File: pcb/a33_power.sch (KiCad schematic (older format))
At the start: 63 parts, among them U3 TPS62095RGTR, U4 TPS62095RGTR, U5 TPS62095RGTR, U6 TPS62095RGTR, U7 AP131-25

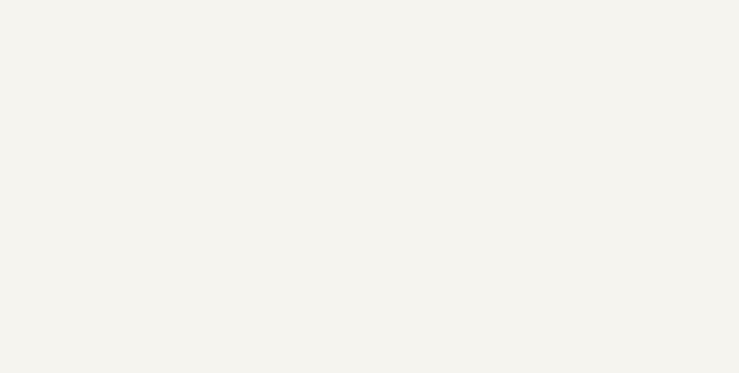
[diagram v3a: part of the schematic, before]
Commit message: Added in the mains to 5V module, this will most likely be removed in the future.
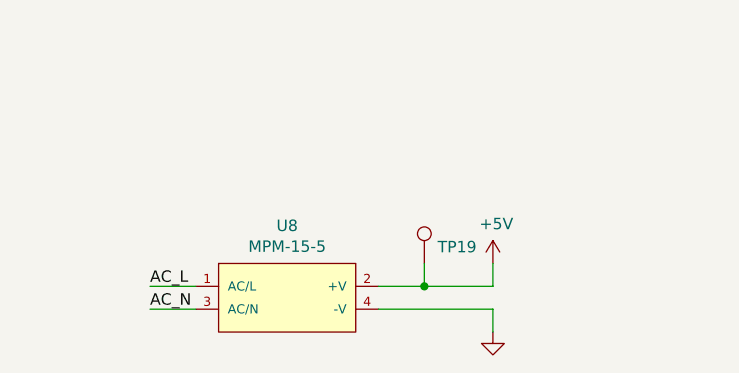
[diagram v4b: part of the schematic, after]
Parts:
- added TP19: TestPoint, TestPoint:TestPoint_Pad_1.0x1.0mm, symbol Connector:TestPoint
- added U8: MPM-15-5, MEAN_WELL-MPM-15-5-*, symbol MPM-15-5:MPM-15-5
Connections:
- net +5V: now also TP19.1, U8.2 (+V)
- net GND: now also U8.4 (-V)
- new net AC_L: U8.1 (AC/L)
- new net AC_N: U8.3 (AC/N)
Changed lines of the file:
@@
 Wire Wire Line
 	4800 5650 4550 5650
+$Comp
+L MPM-15-5:MPM-15-5 U8
+U 1 1 60F3A4A1
+P 1300 6650
+F 0 "U8" H 1800 6915 50  0000 C CNN
+F 1 "MPM-15-5" H 1800 6824 50  0000 C CNN
+F 2 "MEAN_WELL-MPM-15-5-*" H 1300 7050 50  0001 L CNN
+F 3 "https://www.meanwell.com/webapp/product/search.aspx?prod=MPM-15#1" H 1300 7150 50  0001 L CNN
+F 4 "No" H 1300 7250 50  0001 L CNN "automotive"
+F 5 "IC" H 1300 7350 50  0001 L CNN "category"
+F 6 "Integrated Circuits (ICs)" H 1300 7450 50  0001 L CNN "device class L1"
+F 7 "Power Management ICs" H 1300 7550 50  0001 L CNN "device class L2"
+F 8 "unset" H 1300 7650 50  0001 L CNN "device class L3"
+F 9 "AC/DC CONVERTER 5V 15W" H 1300 7750 50  0001 L CNN "digikey description"
+F 10 "1866-5334-ND" H 1300 7850 50  0001 L CNN "digikey part number"
+F 11 "24mm" H 1300 7950 50  0001 L CNN "height"
+F 12 "Yes" H 1300 8050 50  0001 L CNN "lead free"
+F 13 "07bef24d1664adcc" H 1300 8150 50  0001 L CNN "library id"
+F 14 "MEAN WELL" H 1300 8250 50  0001 L CNN "manufacturer"
+F 15 "15W" H 1300 8350 50  0001 L CNN "max power dissipation"
+F 16 "264V" H 1300 8450 50  0001 L CNN "max supply voltage"
+F 17 "80V" H 1300 8550 50  0001 L CNN "min supply voltage"
+F 18 "709-MPM-15-5" H 1300 8650 50  0001 L CNN "mouser part number"
+F 19 "0.3-0.6A" H 1300 8750 50  0001 L CNN "nominal supply current"
+F 20 "1" H 1300 8850 50  0001 L CNN "number of outputs"
+F 21 "3A" H 1300 8950 50  0001 L CNN "output current"
+F 22 "5V" H 1300 9050 50  0001 L CNN "output voltage"
+F 23 "DIP4" H 1300 9150 50  0001 L CNN "package"
+F 24 "Yes" H 1300 9250 50  0001 L CNN "rohs"
+F 25 "+85°C" H 1300 9350 50  0001 L CNN "temperature range high"
+F 26 "-40°C" H 1300 9450 50  0001 L CNN "temperature range low"
+F 27 "MPM-15-5" H 1300 6650 50  0001 C CNN "Part Number"
+	1    1300 6650
+	1    0    0    -1
+$EndComp
+Wire Wire Line
+	1400 6650 1200 6650
+Wire Wire Line
+	1400 6750 1200 6750
+Text Label 1200 6650 0    50   ~ 0
+AC_L
+Text Label 1200 6750 0    50   ~ 0
+AC_N
+$Comp
+L power:+5V #PWR070
+U 1 1 60F7B9D6
+P 2700 6550
+F 0 "#PWR070" H 2700 6400 50  0001 C CNN
+F 1 "+5V" H 2715 6723 50  0000 C CNN
+F 2 "" H 2700 6550 50  0001 C CNN
+F 3 "" H 2700 6550 50  0001 C CNN
+	1    2700 6550
+	1    0    0    -1
+$EndComp
+$Comp
+L power:GND #PWR?
+U 1 1 60F96CCE
+P 2700 6850
+AR Path="/60536DA4/60F96CCE" Ref="#PWR?"  Part="1"
+AR Path="/60F96CCE" Ref="#PWR?"  Part="1"
+AR Path="/60A30BFF/60F96CCE" Ref="#PWR071"  Part="1"
+F 0 "#PWR071" H 2700 6600 50  0001 C CNN
+F 1 "GND" V 2705 6722 50  0001 R CNN
+F 2 "" H 2700 6850 50  0001 C CNN
+F 3 "" H 2700 6850 50  0001 C CNN
+	1    2700 6850
+	1    0    0    -1
+$EndComp
+Wire Wire Line
+	2200 6650 2400 6650
+Wire Wire Line
+	2700 6650 2700 6550
+Wire Wire Line
+	2200 6750 2700 6750
+Wire Wire Line
+	2700 6750 2700 6850
+$Comp
+L Connector:TestPoint TP19
+U 1 1 60FBE2BB
+P 2400 6550
+F 0 "TP19" H 2458 6622 50  0000 L CNN
+F 1 "TestPoint" H 2458 6577 50  0001 L CNN
+F 2 "TestPoint:TestPoint_Pad_1.0x1.0mm" H 2600 6550 50  0001 C CNN
+F 3 "~" H 2600 6550 50  0001 C CNN
+	1    2400 6550
+	1    0    0    -1
+$EndComp
+Wire Wire Line
+	2400 6650 2400 6550
+Connection ~ 2400 6650
+Wire Wire Line
+	2400 6650 2700 6650
 $EndSCHEMATC

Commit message: Figured out all the crystals
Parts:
- U8: footprint MEAN_WELL-MPM-15-5-* -> MPM-15-5:MEAN_WELL-MPM-15-5-MFG
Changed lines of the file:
@@
 F 0 "U8" H 1800 6915 50  0000 C CNN
 F 1 "MPM-15-5" H 1800 6824 50  0000 C CNN
-F 2 "MEAN_WELL-MPM-15-5-*" H 1300 7050 50  0001 L CNN
+F 2 "MPM-15-5:MEAN_WELL-MPM-15-5-MFG" H 1300 7050 50  0001 L CNN
 F 3 "https://www.meanwell.com/webapp/product/search.aspx?prod=MPM-15#1" H 1300 7150 50  0001 L CNN
 F 4 "No" H 1300 7250 50  0001 L CNN "automotive"

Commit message: Backing up
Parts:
- C10, C11, C12, C13, C14, C15, C16, C17, C18, C19, C20, C21, C22, C23, C24, C25, C26, C27, C28, C6, C7, C8, C9: footprint Capacitor_SMD:C_01005_0402Metric -> Capacitor_SMD:C_0402_1005Metric
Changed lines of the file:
@@
 F 0 "C9" H 4250 1300 50  0000 L CNN
 F 1 "22uF" H 4250 1100 50  0000 L CNN
-F 2 "Capacitor_SMD:C_01005_0402Metric" H 4200 1200 50  0001 C CNN
+F 2 "Capacitor_SMD:C_0402_1005Metric" H 4200 1200 50  0001 C CNN
 F 3 "~" H 4200 1200 50  0001 C CNN
 	1    4200 1200
@@
 F 0 "C10" H 4550 1300 50  0000 L CNN
 F 1 "22uF" H 4550 1100 50  0000 L CNN
-F 2 "Capacitor_SMD:C_01005_0402Metric" H 4500 1200 50  0001 C CNN
+F 2 "Capacitor_SMD:C_0402_1005Metric" H 4500 1200 50  0001 C CNN
 F 3 "~" H 4500 1200 50  0001 C CNN
 	1    4500 1200
@@
 F 0 "C7" H 3200 1950 50  0000 L CNN
 F 1 "10nF" H 3200 1750 50  0000 L CNN
-F 2 "Capacitor_SMD:C_01005_0402Metric" H 3150 1850 50  0001 C CNN
+F 2 "Capacitor_SMD:C_0402_1005Metric" H 3150 1850 50  0001 C CNN
 F 3 "~" H 3150 1850 50  0001 C CNN
 	1    3150 1850
@@
 F 0 "C8" H 3200 2550 50  0000 L CNN
 F 1 "450pF" H 3200 2350 50  0000 L CNN
-F 2 "Capacitor_SMD:C_01005_0402Metric" H 3150 2450 50  0001 C CNN
+F 2 "Capacitor_SMD:C_0402_1005Metric" H 3150 2450 50  0001 C CNN
 F 3 "~" H 3150 2450 50  0001 C CNN
 	1    3150 2450
@@
 F 0 "C6" H 950 1300 50  0000 L CNN
 F 1 "22uF" H 950 1100 50  0000 L CNN
-F 2 "Capacitor_SMD:C_01005_0402Metric" H 900 1200 50  0001 C CNN
+F 2 "Capacitor_SMD:C_0402_1005Metric" H 900 1200 50  0001 C CNN
 F 3 "~" H 900 1200 50  0001 C CNN
 	1    900  1200
@@
 F 0 "C14" H 4250 3650 50  0000 L CNN
 F 1 "22uF" H 4250 3450 50  0000 L CNN
-F 2 "Capacitor_SMD:C_01005_0402Metric" H 4200 3550 50  0001 C CNN
+F 2 "Capacitor_SMD:C_0402_1005Metric" H 4200 3550 50  0001 C CNN
 F 3 "~" H 4200 3550 50  0001 C CNN
 	1    4200 3550
@@
 F 0 "C15" H 4550 3650 50  0000 L CNN
 F 1 "22uF" H 4550 3450 50  0000 L CNN
-F 2 "Capacitor_SMD:C_01005_0402Metric" H 4500 3550 50  0001 C CNN
+F 2 "Capacitor_SMD:C_0402_1005Metric" H 4500 3550 50  0001 C CNN
 F 3 "~" H 4500 3550 50  0001 C CNN
 	1    4500 3550
@@
 F 0 "C12" H 3200 4300 50  0000 L CNN
 F 1 "10nF" H 3200 4100 50  0000 L CNN
-F 2 "Capacitor_SMD:C_01005_0402Metric" H 3150 4200 50  0001 C CNN
+F 2 "Capacitor_SMD:C_0402_1005Metric" H 3150 4200 50  0001 C CNN
 F 3 "~" H 3150 4200 50  0001 C CNN
 	1    3150 4200
@@
 F 0 "C13" H 3200 4900 50  0000 L CNN
 F 1 "450pF" H 3200 4700 50  0000 L CNN
-F 2 "Capacitor_SMD:C_01005_0402Metric" H 3150 4800 50  0001 C CNN
+F 2 "Capacitor_SMD:C_0402_1005Metric" H 3150 4800 50  0001 C CNN
 F 3 "~" H 3150 4800 50  0001 C CNN
 	1    3150 4800
@@
 F 0 "C11" H 950 3650 50  0000 L CNN
 F 1 "22uF" H 950 3450 50  0000 L CNN
-F 2 "Capacitor_SMD:C_01005_0402Metric" H 900 3550 50  0001 C CNN
+F 2 "Capacitor_SMD:C_0402_1005Metric" H 900 3550 50  0001 C CNN
 F 3 "~" H 900 3550 50  0001 C CNN
 	1    900  3550
@@
 F 0 "C22" H 9500 1300 50  0000 L CNN
 F 1 "22uF" H 9500 1100 50  0000 L CNN
-F 2 "Capacitor_SMD:C_01005_0402Metric" H 9450 1200 50  0001 C CNN
+F 2 "Capacitor_SMD:C_0402_1005Metric" H 9450 1200 50  0001 C CNN
 F 3 "~" H 9450 1200 50  0001 C CNN
 	1    9450 1200
@@
 F 0 "C24" H 9800 1300 50  0000 L CNN
 F 1 "22uF" H 9800 1100 50  0000 L CNN
-F 2 "Capacitor_SMD:C_01005_0402Metric" H 9750 1200 50  0001 C CNN
+F 2 "Capacitor_SMD:C_0402_1005Metric" H 9750 1200 50  0001 C CNN
 F 3 "~" H 9750 1200 50  0001 C CNN
 	1    9750 1200
@@
 F 0 "C18" H 8450 1950 50  0000 L CNN
 F 1 "10nF" H 8450 1750 50  0000 L CNN
-F 2 "Capacitor_SMD:C_01005_0402Metric" H 8400 1850 50  0001 C CNN
+F 2 "Capacitor_SMD:C_0402_1005Metric" H 8400 1850 50  0001 C CNN
 F 3 "~" H 8400 1850 50  0001 C CNN
 	1    8400 1850
@@
 F 0 "C19" H 8450 2550 50  0000 L CNN
 F 1 "5nF" H 8450 2350 50  0000 L CNN
-F 2 "Capacitor_SMD:C_01005_0402Metric" H 8400 2450 50  0001 C CNN
+F 2 "Capacitor_SMD:C_0402_1005Metric" H 8400 2450 50  0001 C CNN
 F 3 "~" H 8400 2450 50  0001 C CNN
 	1    8400 2450
@@
 F 0 "C16" H 6200 1300 50  0000 L CNN
 F 1 "22uF" H 6200 1100 50  0000 L CNN
-F 2 "Capacitor_SMD:C_01005_0402Metric" H 6150 1200 50  0001 C CNN
+F 2 "Capacitor_SMD:C_0402_1005Metric" H 6150 1200 50  0001 C CNN
 F 3 "~" H 6150 1200 50  0001 C CNN
 	1    6150 1200
@@
 F 0 "C23" H 9500 3500 50  0000 L CNN
 F 1 "22uF" H 9500 3300 50  0000 L CNN
-F 2 "Capacitor_SMD:C_01005_0402Metric" H 9450 3400 50  0001 C CNN
+F 2 "Capacitor_SMD:C_0402_1005Metric" H 9450 3400 50  0001 C CNN
 F 3 "~" H 9450 3400 50  0001 C CNN
 	1    9450 3400
@@
 F 0 "C25" H 9800 3500 50  0000 L CNN
 F 1 "22uF" H 9800 3300 50  0000 L CNN
-F 2 "Capacitor_SMD:C_01005_0402Metric" H 9750 3400 50  0001 C CNN
+F 2 "Capacitor_SMD:C_0402_1005Metric" H 9750 3400 50  0001 C CNN
 F 3 "~" H 9750 3400 50  0001 C CNN
 	1    9750 3400
@@
 F 0 "C20" H 8450 4150 50  0000 L CNN
 F 1 "10nF" H 8450 3950 50  0000 L CNN
-F 2 "Capacitor_SMD:C_01005_0402Metric" H 8400 4050 50  0001 C CNN
+F 2 "Capacitor_SMD:C_0402_1005Metric" H 8400 4050 50  0001 C CNN
 F 3 "~" H 8400 4050 50  0001 C CNN
 	1    8400 4050
@@
 F 0 "C21" H 8450 4750 50  0000 L CNN
 F 1 "5nF" H 8450 4550 50  0000 L CNN
-F 2 "Capacitor_SMD:C_01005_0402Metric" H 8400 4650 50  0001 C CNN
+F 2 "Capacitor_SMD:C_0402_1005Metric" H 8400 4650 50  0001 C CNN
 F 3 "~" H 8400 4650 50  0001 C CNN
 	1    8400 4650
@@
 F 0 "C17" H 6200 3500 50  0000 L CNN
 F 1 "22uF" H 6200 3300 50  0000 L CNN
-F 2 "Capacitor_SMD:C_01005_0402Metric" H 6150 3400 50  0001 C CNN
+F 2 "Capacitor_SMD:C_0402_1005Metric" H 6150 3400 50  0001 C CNN
 F 3 "~" H 6150 3400 50  0001 C CNN
 	1    6150 3400
@@
 F 0 "C28" H 6000 6050 50  0000 L CNN
 F 1 "10uF" H 6000 5850 50  0000 L CNN
-F 2 "Capacitor_SMD:C_01005_0402Metric" H 5950 5950 50  0001 C CNN
+F 2 "Capacitor_SMD:C_0402_1005Metric" H 5950 5950 50  0001 C CNN
 F 3 "~" H 5950 5950 50  0001 C CNN
 	1    5950 5950
@@
 F 0 "C27" H 5650 6050 50  0000 L CNN
 F 1 "0.1uF" H 5650 5850 50  0000 L CNN
-F 2 "Capacitor_SMD:C_01005_0402Metric" H 5600 5950 50  0001 C CNN
+F 2 "Capacitor_SMD:C_0402_1005Metric" H 5600 5950 50  0001 C CNN
 F 3 "~" H 5600 5950 50  0001 C CNN
 	1    5600 5950
@@
 F 0 "C26" H 4600 5950 50  0000 L CNN
 F 1 "10uF" H 4600 5750 50  0000 L CNN
-F 2 "Capacitor_SMD:C_01005_0402Metric" H 4550 5850 50  0001 C CNN
+F 2 "Capacitor_SMD:C_0402_1005Metric" H 4550 5850 50  0001 C CNN
 F 3 "~" H 4550 5850 50  0001 C CNN
 	1    4550 5850

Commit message: Working on the layout
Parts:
- removed TP19, TP4, TP7, TP8: TestPoint, TestPoint:TestPoint_Pad_1.0x1.0mm, symbol Connector:TestPoint
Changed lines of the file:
@@
 Connection ~ 900  3350
-Wire Wire Line
-	900  3350 1150 3350
 Wire Wire Line
 	900  3650 900  3750
@@
 Wire Wire Line
 	4700 3350 4700 3200
-$Comp
-L Connector:TestPoint TP4
-U 1 1 60A665AC
-P 1150 3200
-F 0 "TP4" H 1208 3272 50  0000 L CNN
-F 1 "TestPoint" H 1208 3227 50  0001 L CNN
-F 2 "TestPoint:TestPoint_Pad_1.0x1.0mm" H 1350 3200 50  0001 C CNN
-F 3 "~" H 1350 3200 50  0001 C CNN
-	1    1150 3200
-	1    0    0    -1
-$EndComp
-Wire Wire Line
-	1150 3350 1150 3200
-Connection ~ 1150 3350
-Wire Wire Line
-	1150 3350 1350 3350
 $Comp
 L power:+5V #PWR029
@@
 Connection ~ 6150 1000
 Wire Wire Line
-	6150 1000 6400 1000
-Wire Wire Line
 	6150 1300 6150 1400
 $Comp
@@
 Wire Wire Line
 	9950 1000 9950 850
-$Comp
-L Connector:TestPoint TP7
-U 1 1 60A89518
-P 6400 850
-F 0 "TP7" H 6458 922 50  0000 L CNN
-F 1 "TestPoint" H 6458 877 50  0001 L CNN
-F 2 "TestPoint:TestPoint_Pad_1.0x1.0mm" H 6600 850 50  0001 C CNN
-F 3 "~" H 6600 850 50  0001 C CNN
-	1    6400 850
-	1    0    0    -1
-$EndComp
-Wire Wire Line
-	6400 1000 6400 850
-Connection ~ 6400 1000
-Wire Wire Line
-	6400 1000 6600 1000
 $Comp
 L power:+5V #PWR030
@@
 Connection ~ 6150 3200
 Wire Wire Line
-	6150 3200 6400 3200
-Wire Wire Line
 	6150 3500 6150 3600
 $Comp
@@
 Wire Wire Line
 	9950 3200 9950 3050
-$Comp
-L Connector:TestPoint TP8
-U 1 1 60C5312A
-P 6400 3050
-F 0 "TP8" H 6458 3122 50  0000 L CNN
-F 1 "TestPoint" H 6458 3077 50  0001 L CNN
-F 2 "TestPoint:TestPoint_Pad_1.0x1.0mm" H 6600 3050 50  0001 C CNN
-F 3 "~" H 6600 3050 50  0001 C CNN
-	1    6400 3050
-	1    0    0    -1
-$EndComp
-Wire Wire Line
-	6400 3200 6400 3050
-Connection ~ 6400 3200
-Wire Wire Line
-	6400 3200 6600 3200
 $Comp
 L power:+3V0 #PWR028
@@
 $EndComp
 Wire Wire Line
-	2200 6650 2400 6650
-Wire Wire Line
 	2700 6650 2700 6550
 Wire Wire Line
@@
 Wire Wire Line
 	2700 6750 2700 6850
-$Comp
-L Connector:TestPoint TP19
-U 1 1 60FBE2BB
-P 2400 6550
-F 0 "TP19" H 2458 6622 50  0000 L CNN
-F 1 "TestPoint" H 2458 6577 50  0001 L CNN
-F 2 "TestPoint:TestPoint_Pad_1.0x1.0mm" H 2600 6550 50  0001 C CNN
-F 3 "~" H 2600 6550 50  0001 C CNN
-	1    2400 6550
-	1    0    0    -1
-$EndComp
-Wire Wire Line
-	2400 6650 2400 6550
-Connection ~ 2400 6650
-Wire Wire Line
-	2400 6650 2700 6650
+Wire Wire Line
+	900  3350 1350 3350
+Wire Wire Line
+	6150 3200 6600 3200
+Wire Wire Line
+	6150 1000 6600 1000
+Wire Wire Line
+	2200 6650 2700 6650
 $EndSCHEMATC

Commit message: Working on the power supplies
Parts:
- removed TP10, TP2, TP5, TP9: TestPoint, TestPoint:TestPoint_Pad_1.0x1.0mm, symbol Connector:TestPoint
- C10, C11, C14, C15, C16, C17, C22, C23, C24, C25, C26, C28, C6, C9: footprint Capacitor_SMD:C_0402_1005Metric -> Capacitor_SMD:C_0805_2012Metric
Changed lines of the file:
@@
 	1350 2100 1350 1300
 Connection ~ 1350 1300
-$Comp
-L Connector:TestPoint TP2
-U 1 1 6077F3FF
-P 1450 1800
-F 0 "TP2" H 1508 1872 50  0000 L CNN
-F 1 "TestPoint" H 1508 1827 50  0001 L CNN
-F 2 "TestPoint:TestPoint_Pad_1.0x1.0mm" H 1650 1800 50  0001 C CNN
-F 3 "~" H 1650 1800 50  0001 C CNN
-	1    1450 1800
-	1    0    0    -1
-$EndComp
 Connection ~ 1350 1000
 Wire Wire Line
@@
 Wire Wire Line
 	1350 2100 1550 2100
-Wire Wire Line
-	1550 1900 1450 1900
-Wire Wire Line
-	1450 1900 1450 1800
 Wire Wire Line
 	2950 1100 3050 1100
@@
 F 0 "C9" H 4250 1300 50  0000 L CNN
 F 1 "22uF" H 4250 1100 50  0000 L CNN
-F 2 "Capacitor_SMD:C_0402_1005Metric" H 4200 1200 50  0001 C CNN
+F 2 "Capacitor_SMD:C_0805_2012Metric" H 4200 1200 50  0001 C CNN
 F 3 "~" H 4200 1200 50  0001 C CNN
 	1    4200 1200
@@
 F 0 "C10" H 4550 1300 50  0000 L CNN
 F 1 "22uF" H 4550 1100 50  0000 L CNN
-F 2 "Capacitor_SMD:C_0402_1005Metric" H 4500 1200 50  0001 C CNN
+F 2 "Capacitor_SMD:C_0805_2012Metric" H 4500 1200 50  0001 C CNN
 F 3 "~" H 4500 1200 50  0001 C CNN
 	1    4500 1200
@@
 F 0 "C6" H 950 1300 50  0000 L CNN
 F 1 "22uF" H 950 1100 50  0000 L CNN
-F 2 "Capacitor_SMD:C_0402_1005Metric" H 900 1200 50  0001 C CNN
+F 2 "Capacitor_SMD:C_0805_2012Metric" H 900 1200 50  0001 C CNN
 F 3 "~" H 900 1200 50  0001 C CNN
 	1    900  1200
@@
 	1350 4450 1350 3650
 Connection ~ 1350 3650
-$Comp
-L Connector:TestPoint TP5
-U 1 1 60A66511
-P 1450 4150
-F 0 "TP5" H 1508 4222 50  0000 L CNN
-F 1 "TestPoint" H 1508 4177 50  0001 L CNN
-F 2 "TestPoint:TestPoint_Pad_1.0x1.0mm" H 1650 4150 50  0001 C CNN
-F 3 "~" H 1650 4150 50  0001 C CNN
-	1    1450 4150
-	1    0    0    -1
-$EndComp
 Connection ~ 1350 3350
 Wire Wire Line
@@
 Wire Wire Line
 	1350 4450 1550 4450
-Wire Wire Line
-	1550 4250 1450 4250
-Wire Wire Line
-	1450 4250 1450 4150
 Wire Wire Line
 	2950 3450 3050 3450
@@
 F 0 "C14" H 4250 3650 50  0000 L CNN
 F 1 "22uF" H 4250 3450 50  0000 L CNN
-F 2 "Capacitor_SMD:C_0402_1005Metric" H 4200 3550 50  0001 C CNN
+F 2 "Capacitor_SMD:C_0805_2012Metric" H 4200 3550 50  0001 C CNN
 F 3 "~" H 4200 3550 50  0001 C CNN
 	1    4200 3550
@@
 F 0 "C15" H 4550 3650 50  0000 L CNN
 F 1 "22uF" H 4550 3450 50  0000 L CNN
-F 2 "Capacitor_SMD:C_0402_1005Metric" H 4500 3550 50  0001 C CNN
+F 2 "Capacitor_SMD:C_0805_2012Metric" H 4500 3550 50  0001 C CNN
 F 3 "~" H 4500 3550 50  0001 C CNN
 	1    4500 3550
@@
 F 0 "C11" H 950 3650 50  0000 L CNN
 F 1 "22uF" H 950 3450 50  0000 L CNN
-F 2 "Capacitor_SMD:C_0402_1005Metric" H 900 3550 50  0001 C CNN
+F 2 "Capacitor_SMD:C_0805_2012Metric" H 900 3550 50  0001 C CNN
 F 3 "~" H 900 3550 50  0001 C CNN
 	1    900  3550
@@
 	6600 2100 6600 1300
 Connection ~ 6600 1300
-$Comp
-L Connector:TestPoint TP9
-U 1 1 60A8947D
-P 6700 1800
-F 0 "TP9" H 6758 1872 50  0000 L CNN
-F 1 "TestPoint" H 6758 1827 50  0001 L CNN
-F 2 "TestPoint:TestPoint_Pad_1.0x1.0mm" H 6900 1800 50  0001 C CNN
-F 3 "~" H 6900 1800 50  0001 C CNN
-	1    6700 1800
-	1    0    0    -1
-$EndComp
 Connection ~ 6600 1000
 Wire Wire Line
@@
 Wire Wire Line
 	6600 2100 6800 2100
-Wire Wire Line
-	6800 1900 6700 1900
-Wire Wire Line
-	6700 1900 6700 1800
 Wire Wire Line
 	8200 1100 8300 1100
@@
 F 0 "C22" H 9500 1300 50  0000 L CNN
 F 1 "22uF" H 9500 1100 50  0000 L CNN
-F 2 "Capacitor_SMD:C_0402_1005Metric" H 9450 1200 50  0001 C CNN
+F 2 "Capacitor_SMD:C_0805_2012Metric" H 9450 1200 50  0001 C CNN
 F 3 "~" H 9450 1200 50  0001 C CNN
 	1    9450 1200
@@
 F 0 "C24" H 9800 1300 50  0000 L CNN
 F 1 "22uF" H 9800 1100 50  0000 L CNN
-F 2 "Capacitor_SMD:C_0402_1005Metric" H 9750 1200 50  0001 C CNN
+F 2 "Capacitor_SMD:C_0805_2012Metric" H 9750 1200 50  0001 C CNN
 F 3 "~" H 9750 1200 50  0001 C CNN
 	1    9750 1200
@@
 Wire Wire Line
 	8400 2100 8400 2350
-$Comp
-L TI:TPS62095 U5
-U 1 1 60A894ED
-P 7500 1550
-F 0 "U5" H 7500 2387 60  0000 C CNN
-F 1 "TPS62095RGTR" H 7500 2281 60  0000 C CNN
-F 2 "TI:TI_RTE_S-PWQFN-N16" H 7500 1750 60  0001 C CNN
-F 3 "" H 7500 1750 60  0001 C CNN
-	1    7500 1550
-	1    0    0    -1
-$EndComp
 Wire Notes Line
 	8700 2250 7900 2250
@@
 F 0 "C16" H 6200 1300 50  0000 L CNN
 F 1 "22uF" H 6200 1100 50  0000 L CNN
-F 2 "Capacitor_SMD:C_0402_1005Metric" H 6150 1200 50  0001 C CNN
+F 2 "Capacitor_SMD:C_0805_2012Metric" H 6150 1200 50  0001 C CNN
 F 3 "~" H 6150 1200 50  0001 C CNN
 	1    6150 1200
@@
 	6600 4300 6600 3500
 Connection ~ 6600 3500
-$Comp
-L Connector:TestPoint TP10
-U 1 1 60C5308F
-P 6700 4000
-F 0 "TP10" H 6758 4072 50  0000 L CNN
-F 1 "TestPoint" H 6758 4027 50  0001 L CNN
-F 2 "TestPoint:TestPoint_Pad_1.0x1.0mm" H 6900 4000 50  0001 C CNN
-F 3 "~" H 6900 4000 50  0001 C CNN
-	1    6700 4000
-	1    0    0    -1
-$EndComp
 Connection ~ 6600 3200
 Wire Wire Line
@@
 Wire Wire Line
 	6600 4300 6800 4300
-Wire Wire Line
-	6800 4100 6700 4100
-Wire Wire Line
-	6700 4100 6700 4000
 Wire Wire Line
 	8200 3300 8300 3300
@@
 F 0 "C23" H 9500 3500 50  0000 L CNN
 F 1 "22uF" H 9500 3300 50  0000 L CNN
-F 2 "Capacitor_SMD:C_0402_1005Metric" H 9450 3400 50  0001 C CNN
+F 2 "Capacitor_SMD:C_0805_2012Metric" H 9450 3400 50  0001 C CNN
 F 3 "~" H 9450 3400 50  0001 C CNN
 	1    9450 3400
@@
 F 0 "C25" H 9800 3500 50  0000 L CNN
 F 1 "22uF" H 9800 3300 50  0000 L CNN
-F 2 "Capacitor_SMD:C_0402_1005Metric" H 9750 3400 50  0001 C CNN
+F 2 "Capacitor_SMD:C_0805_2012Metric" H 9750 3400 50  0001 C CNN
 F 3 "~" H 9750 3400 50  0001 C CNN
 	1    9750 3400
@@
 F 0 "C17" H 6200 3500 50  0000 L CNN
 F 1 "22uF" H 6200 3300 50  0000 L CNN
-F 2 "Capacitor_SMD:C_0402_1005Metric" H 6150 3400 50  0001 C CNN
+F 2 "Capacitor_SMD:C_0805_2012Metric" H 6150 3400 50  0001 C CNN
 F 3 "~" H 6150 3400 50  0001 C CNN
 	1    6150 3400
@@
 F 0 "C28" H 6000 6050 50  0000 L CNN
 F 1 "10uF" H 6000 5850 50  0000 L CNN
-F 2 "Capacitor_SMD:C_0402_1005Metric" H 5950 5950 50  0001 C CNN
+F 2 "Capacitor_SMD:C_0805_2012Metric" H 5950 5950 50  0001 C CNN
 F 3 "~" H 5950 5950 50  0001 C CNN
 	1    5950 5950
@@
 F 0 "C26" H 4600 5950 50  0000 L CNN
 F 1 "10uF" H 4600 5750 50  0000 L CNN
-F 2 "Capacitor_SMD:C_0402_1005Metric" H 4550 5850 50  0001 C CNN
+F 2 "Capacitor_SMD:C_0805_2012Metric" H 4550 5850 50  0001 C CNN
 F 3 "~" H 4550 5850 50  0001 C CNN
 	1    4550 5850
@@
 Wire Wire Line
 	2200 6650 2700 6650
+$Comp
+L TI:TPS62095 U5
+U 1 1 60A894ED
+P 7500 1550
+F 0 "U5" H 7500 2387 60  0000 C CNN
+F 1 "TPS62095RGTR" H 7500 2281 60  0000 C CNN
+F 2 "TI:TI_RTE_S-PWQFN-N16" H 7500 1750 60  0001 C CNN
+F 3 "" H 7500 1750 60  0001 C CNN
+	1    7500 1550
+	1    0    0    -1
+$EndComp
 $EndSCHEMATC
